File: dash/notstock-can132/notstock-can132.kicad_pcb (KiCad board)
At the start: 2 copper layers, 34.4 x 34.4 mm, 28 parts, among them J1 OBD 12V GND H L, J2 wires from the display, U1 LMR16006YDDCR, U2 SN65HVD230

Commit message: CAN boards: D3 K16 (C2943756) for the PMEG6010CEH out of stock
Same footprint (SOD-123FL on the SOD-123F pads), 60 V 1 A Schottky.
BOM, schematic and the boards' LCSC fields updated on both boards.

Co-Authored-By: Claude Opus 5.5 <noreply@anthropic.com>
Claude-Session: https://claude.ai/code/session_018SKN4tJhAPpVCWtvRZgZpD
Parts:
- D3: value PMEG6010CEH -> K16
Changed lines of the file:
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@@
     (descr "D_SOD-123F")
     (tags "D_SOD-123F")
-    (property "LCSC" "C110797")
+    (property "LCSC" "C2943756")
     (attr smd)
     (fp_text reference "D3" (at -0.0225 1.875) (layer "F.SilkS")
         (effects (font (size 0.8 0.8) (thickness 0.13)))
     )
-    (fp_text value "PMEG6010CEH" (at 0 2.1) (layer "F.Fab") hide
+    (fp_text value "K16" (at 0 2.1) (layer "F.Fab") hide
         (effects (font (size 1 1) (thickness 0.15)))
     )

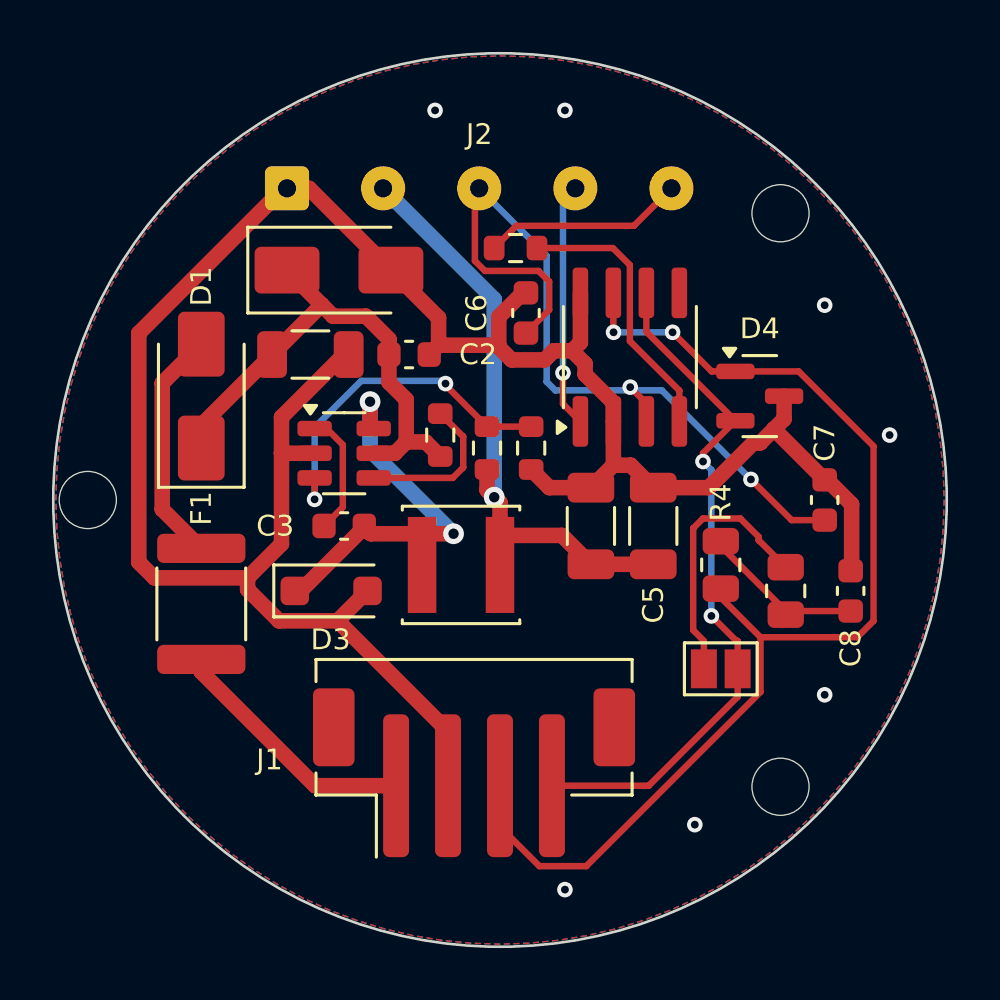
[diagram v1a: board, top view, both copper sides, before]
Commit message: CAN boards: JLCPCB basic parts where possible
D1 SS16 -> SS34 (C8678, basic, same SMA footprint) on both boards.
CAN 1.32: C4/C5 22 uF 1206 -> 0805 25 V (C45783, basic), rerouted,
DRC clean.

Co-Authored-By: Claude Opus 5.5 <noreply@anthropic.com>
Claude-Session: https://claude.ai/code/session_018SKN4tJhAPpVCWtvRZgZpD
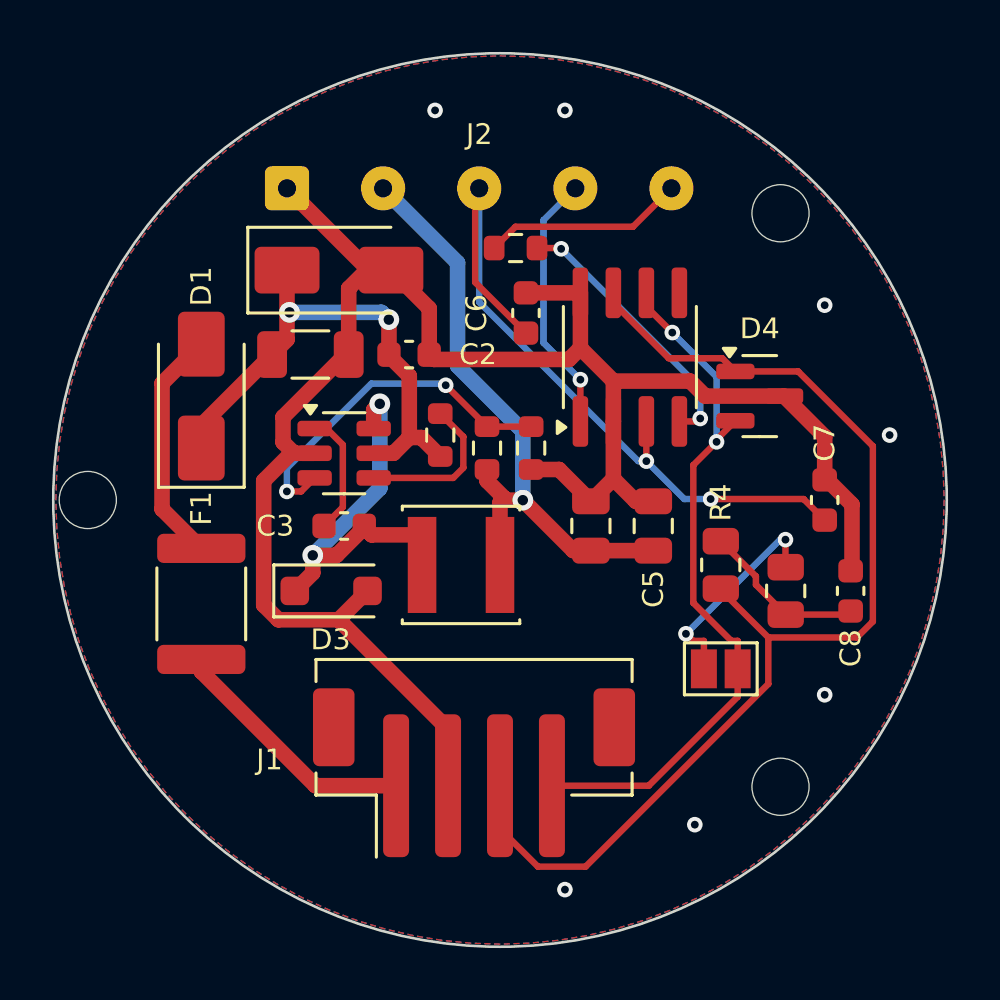
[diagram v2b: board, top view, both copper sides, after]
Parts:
- C4, C5: value 22u 16V -> 22u 25V; footprint Capacitor_SMD:C_1206_3216Metric -> Capacitor_SMD:C_0805_2012Metric
- D1: value SS16 -> SS34
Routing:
- net GND: track 91.5 -> 74.3 mm
- net +3V3: track 31.5 -> 29.1 mm
- net TERM: track 10.2 -> 8.28 mm, vias 0 -> 2
- net CANL: track 26.6 -> 27.6 mm
- net VSYS: track 23.9 -> 24.8 mm
- net CANH: track 44.3 -> 43.6 mm, vias 2 -> 0
- net TXD: track 9.45 -> 10.1 mm
- net VIN: track 19.7 -> 20.2 mm, vias 0 -> 2
- net RXD_T: track 10.7 -> 10.5 mm, vias 0 -> 2
